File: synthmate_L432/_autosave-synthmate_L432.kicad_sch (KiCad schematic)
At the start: 45 parts, among them J1 USB_C_synthmate, J2 DIN-5_180degree, J3 USB_C_connector_board, J4 DIN-5_180degree, J5 Conn_01x16, J6 Conn_01x13, J7 Conn_01x04, J8 Conn_ST_STDC14, SW1 RotaryEncoder_Switch, SW2 SW_Push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

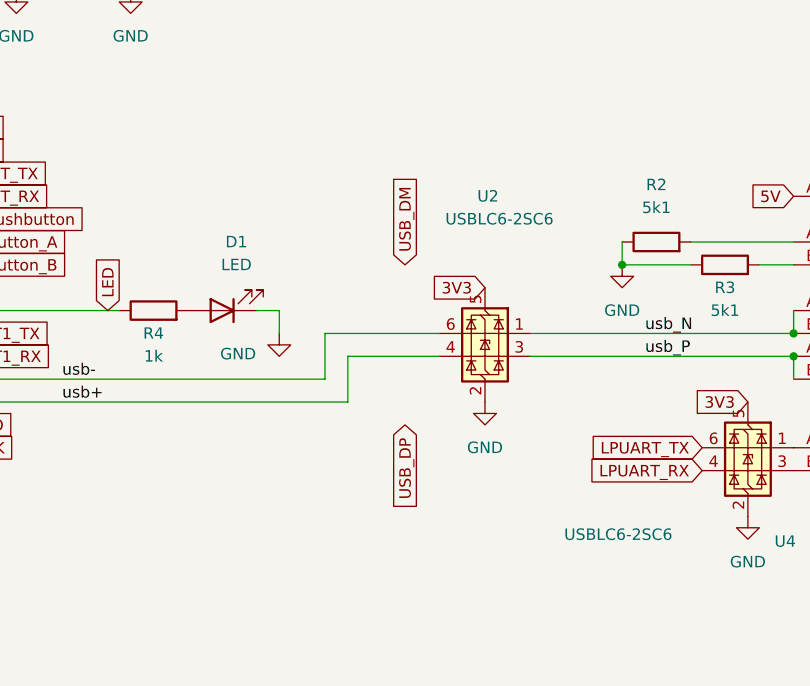
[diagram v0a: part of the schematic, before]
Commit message: moved smd to bottom side, changed back to eusblc6
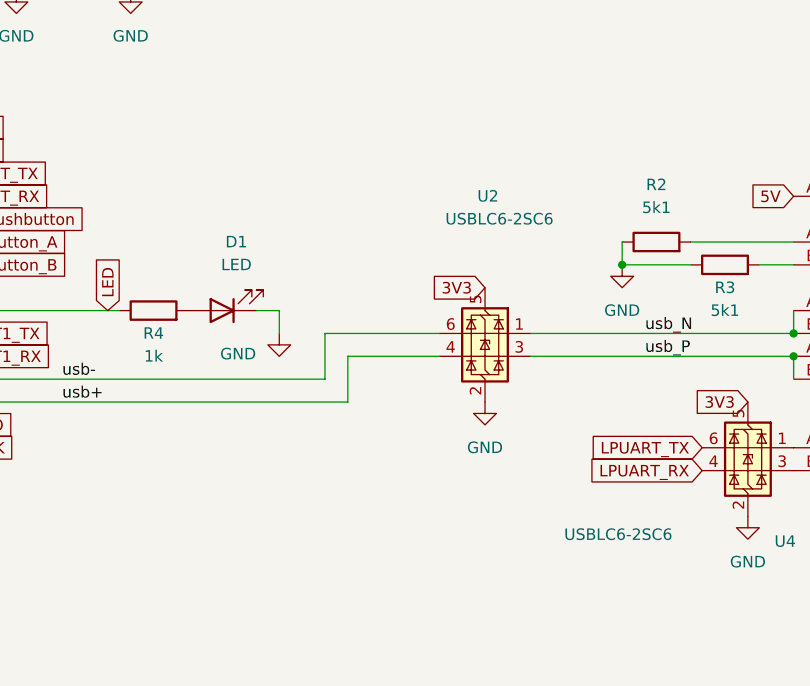
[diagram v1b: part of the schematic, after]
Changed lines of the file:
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@@
-		)
-	)
-	(global_label "USB_DP"
-		(shape input)
-		(at 345.44 106.68 270)
-		(fields_autoplaced yes)
-		(effects
-			(font
-				(size 1.27 1.27)
-			)
-			(justify right)
-		)
-		(property "Intersheetrefs" "${INTERSHEET_REFS}"
-			(at 345.44 116.9828 90)
-			(effects
-				(font
-					(size 1.27 1.27)
-				)
-				(justify right)
-				(hide yes)
-			)
 		)
 	)
@@
 				(hide yes)
 			)
-		)
-	)
-	(global_label "USB_DM"
-		(shape input)
-		(at 345.44 88.9 90)
-		(fields_autoplaced yes)
-		(effects
-			(font
-				(size 1.27 1.27)
-			)
-			(justify left)
-		)
-		(property "Intersheetrefs" "${INTERSHEET_REFS}"
-			(at 345.44 78.4158 90)
-			(effects
-				(font
-					(size 1.27 1.27)
-				)
-				(justify left)
-				(hide yes)
-			)
